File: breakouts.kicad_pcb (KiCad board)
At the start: 2 copper layers, 0 parts

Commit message: Start PCB placing
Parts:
- added C1001: 100nF, SMD0805, F.Cu at (107.0, 62.0)
- added C1101: 100nF, SMD0805, F.Cu at (93.0, 99.0)
- added C1102: 4.7uF, SMD0805, F.Cu at (99.0, 99.0)
- added C1103: 47pF, SMD0805, F.Cu at (106.0, 99.0)
- added C1104: 47pF, SMD0805, F.Cu at (112.0, 99.0)
- added C1105: 47pF, SMD0805, F.Cu at (117.0, 99.0)
- added C1201: 100nF, SMD0805, F.Cu at (163.0, 49.0)
- added C1202: 1000uF 25V, C_radial_10mm, F.Cu at (141.0, 20.0)
- added C1203: 100nF, SMD0805, F.Cu at (157.0, 49.0)
- added C1204: 1000uF 16V, C_radial_10mm, F.Cu at (153.0, 20.0)
- added C1205: 100nF, SMD0805, F.Cu at (151.0, 49.0)
- added C1206: 1000uF 16V, C_radial_10mm, F.Cu at (165.0, 20.0)
- added C1207: 100uF, SMD0805, F.Cu at (145.0, 49.0)
- added C1301: 22pF, SMD0805, F.Cu at (192.0, 21.0)
- added C1302: 22pF, SMD0805, F.Cu at (186.0, 21.0)
- added C1303: 100nF, SMD0805, F.Cu at (180.0, 21.0)
- added C201: 10uF, SMD0805, F.Cu at (35.0, 37.0)
- added C301: 100nF, SMD0805, F.Cu at (53.0, 63.0)
- added C302: 4.7uF, SMD0805, F.Cu at (47.0, 63.0)
- added C303: 47pF, SMD0805, F.Cu at (41.0, 63.0)
- added C304: 47pF, SMD0805, F.Cu at (37.0, 63.0)
- added C305: 47pF, SMD0805, F.Cu at (32.0, 63.0)
- added C401: 47pF, SMD0805, F.Cu at (56.0, 104.0)
- added C402: 0.01µF, SMD0805, F.Cu at (50.0, 104.0)
- added C403: 2.2µF, SMD0805, F.Cu at (43.0, 104.0)
- added C404: 1nF, SMD0805, F.Cu at (37.0, 104.0)
- added C405: 1.2pF, SMD0805, F.Cu at (32.0, 104.0)
- added C406: 27pF, SMD0805, F.Cu at (26.0, 104.0)
- added C407: 2.7pF, SMD0805, F.Cu at (20.0, 104.0)
- added C501: 22µF, SMD0805, F.Cu at (46.0, 119.0)
- added C502: Open, SMD0805, F.Cu at (41.0, 119.0)
- added C503: 22µF, SMD0805, F.Cu at (36.0, 119.0)
- added C601: 10µF, SMD0805, F.Cu at (34.0, 137.0)
- added C602: 10µF, SMD0805, F.Cu at (28.0, 137.0)
- added C701: 100nF, SMD0805, F.Cu at (50.0, 155.0)
- added C702: 100nF, SMD0805, F.Cu at (45.0, 155.0)
- added C703: 22pF, SMD0805, F.Cu at (39.0, 155.0)
- added C704: 22pF, SMD0805, F.Cu at (34.0, 155.0)
- added C801: 100nF, SMD0805, F.Cu at (54.0, 182.0)
- added C802: 100nF, SMD0805, F.Cu at (60.0, 182.0)
- added C803: 1uF, SMD0805, F.Cu at (66.0, 182.0)
- added C804: 22pF, SMD0805, F.Cu at (71.0, 182.0)
- added C805: 22pF, SMD0805, F.Cu at (76.0, 182.0)
- added C901: 100nF, SMD0805, F.Cu at (103.0, 36.0)
- added D1101: LED, LED-0805, F.Cu at (128.0, 95.0)
- added D1102: LED, LED-0805, F.Cu at (122.0, 95.0)
- added D201: PWR, LED-0805, F.Cu at (41.0, 28.0)
- added D202: 3V6, SOD123F, F.Cu at (22.0, 28.0)
- added D203: 3V6, SOD123F, F.Cu at (28.0, 28.0)
- added D301: LED, LED-0805, F.Cu at (34.0, 58.0)
- added D302: LED, LED-0805, F.Cu at (39.0, 58.0)
- added D501: DIODESCH, SOD-123, F.Cu at (42.0, 123.0)
- added D701: RESET, LED-0805, F.Cu at (52.0, 150.0)
- added D702: POWER, LED-0805, F.Cu at (58.0, 150.0)
- added D801: RESET, LED-0805, F.Cu at (84.0, 187.0)
- added D802: POWER, LED-0805, F.Cu at (79.0, 187.0)
- added D901: RESET, LED-0805, F.Cu at (115.0, 35.0)
- added D902: POWER, LED-0805, F.Cu at (110.0, 35.0)
- added IC901: ATTINY85-S, SOIC-8, F.Cu at (94.0, 23.0)
- added J1101: USB_MINI-B, mini-USB, F.Cu at (108.0, 86.0)
- added J1201: JACK_5P, JACK_3.5mm, F.Cu at (123.0, 39.0)
- added J201: USB_MINI-B, mini-USB, F.Cu at (26.0, 37.0)
- added J301: USB_MINI-B, mini-USB, F.Cu at (22.0, 61.0)
- added J401: SMA, PCBedge_SMA, F.Cu at (31.0, 90.0)
- added J801: USB_MINI-B, mini-USB, F.Cu at (93.0, 190.0)
- added K1201: CONN_3, pin_array_3x1, F.Cu at (166.0, 29.0)
- added K1301: CONN_3, pin_array_3x1, F.Cu at (195.0, 17.0)
- added K601: CONN_3, pin_array_3x1, F.Cu at (31.0, 132.0)
- added K801: CONN_3, pin_array_3x1, F.Cu at (36.0, 178.0)
- added L401: 100nH, SMD0805, F.Cu at (53.0, 98.0)
- added L402: 8.2nH, SMD0805, F.Cu at (47.0, 98.0)
- added L403: 22nH, SMD0805, F.Cu at (41.0, 98.0)
- added L501: 22µH, Shielded_inductor, F.Cu at (30.0, 119.0)
- added P1001: CONN_4, pin_array_4x1, F.Cu at (107.0, 69.0)
- added P1002: CONN_4, pin_array_4x1, F.Cu at (96.0, 69.0)
- added P1101: CONN_6, pin_array_6x1, F.Cu at (125.0, 84.0)
- added P1102: CONN_6, pin_array_6x1, F.Cu at (125.0, 89.0)
- added P1201: CONN_2, Screw_Terminal_Block_2P, F.Cu at (165.0, 40.0)
- added P1202: CONN_2, Screw_Terminal_Block_2P, F.Cu at (155.0, 40.0)
- added P1203: CONN_2, Screw_Terminal_Block_2P, F.Cu at (145.0, 40.0)
- added P1301: CONN_2, pin_array_2x1, F.Cu at (181.0, 25.0)
- added P201: CONN_2, pin_array_2x1, F.Cu at (34.0, 28.0)
- added P202: CONN_2, pin_array_2x1, F.Cu at (42.0, 34.0)
- added P203: CONN_2, pin_array_2x1, F.Cu at (50.0, 34.0)
- added P301: CONN_6, pin_array_6x1, F.Cu at (45.0, 72.0)
- added P302: CONN_6, pin_array_6x1, F.Cu at (45.0, 77.0)
- added P401: CONN_8, pin_array_8x1, F.Cu at (26.0, 109.0)
- added P402: CONN_8, pin_array_8x1, F.Cu at (47.0, 110.0)
- added P501: CONN_2, pin_array_2x1, F.Cu at (56.0, 123.0)
- added P502: CONN_2, pin_array_2x1, F.Cu at (49.0, 123.0)
- added P701: POWER, pin_array_8x1, F.Cu at (68.0, 164.0)
- added P702: PORT B, pin_array_8x1, F.Cu at (47.0, 164.0)
- added P703: PORT C, pin_array_8x1, F.Cu at (25.0, 164.0)
- added P704: PORT D, pin_array_8x1, F.Cu at (90.0, 164.0)
- added P705: ISP, pin_array_3x2, F.Cu at (58.0, 158.0)
- added P801: PORT B, pin_array_8x1, F.Cu at (69.0, 192.0)
- added P802: PORT C, pin_array_8x1, F.Cu at (48.0, 192.0)
- added P803: PORT D, pin_array_8x1, F.Cu at (26.0, 192.0)
- added P804: ISP, pin_array_3x2, F.Cu at (35.0, 186.0)
- added P901: CONN_8, pin_array_8x1, F.Cu at (99.0, 30.0)
- added P902: ISP, pin_array_3x2, F.Cu at (92.0, 36.0)
- added R1101: 270R, SMD0603, F.Cu at (92.0, 104.0)
- added R1102: 270R, SMD0603, F.Cu at (99.0, 104.0)
- added R1103: 0R, SMD0603, F.Cu at (105.0, 104.0)
- added R1104: 27R, SMD0603, F.Cu at (111.0, 104.0)
- added R1105: 27R, SMD0603, F.Cu at (117.0, 104.0)
- added R1201: 10k, SMD0603, F.Cu at (186.0, 32.0)
- added R1202: 8.2k, SMD0603, F.Cu at (192.0, 32.0)
- added R1301: 10k, SMD0603, F.Cu at (199.0, 32.0)
- added R1302: 2.2k, SMD0603, F.Cu at (205.0, 32.0)
- added R1303: 2.2k, SMD0603, F.Cu at (211.0, 32.0)
- added R201: 1k, SMD0603, F.Cu at (41.0, 47.0)
- added R202: 1k5, SMD0603, F.Cu at (36.0, 47.0)
- added R203: 68R, SMD0603, F.Cu at (30.0, 47.0)
- added R204: 68R, SMD0603, F.Cu at (25.0, 47.0)
- added R205: 1M, SMD0603, F.Cu at (20.0, 47.0)
- added R301: 270R, SMD0603, F.Cu at (53.0, 67.0)
- added R302: 270R, SMD0603, F.Cu at (47.0, 67.0)
- added R303: 0R, SMD0603, F.Cu at (42.0, 67.0)
- added R304: 27R, SMD0603, F.Cu at (37.0, 67.0)
- added R305: 27R, SMD0603, F.Cu at (32.0, 67.0)
- added R501: 0R, SMD0603, F.Cu at (36.0, 123.0)
- added R701: 1k, SMD0603, F.Cu at (46.0, 150.0)
- added R702: 1k, SMD0603, F.Cu at (41.0, 150.0)
- added R703: 10k, SMD0603, F.Cu at (35.0, 150.0)
- added R801: 22R, SMD0603, F.Cu at (72.0, 186.0)
- added R802: 22R, SMD0603, F.Cu at (68.0, 186.0)
- added R803: 1k, SMD0603, F.Cu at (54.0, 186.0)
- added R804: 1k, SMD0603, F.Cu at (59.0, 186.0)
- added R805: 10k, SMD0603, F.Cu at (64.0, 186.0)
- added R901: 1k, SMD0603, F.Cu at (93.0, 43.0)
- added R902: 1k, SMD0603, F.Cu at (98.0, 43.0)
- added R903: 10k, SMD0603, F.Cu at (104.0, 43.0)
- added SW701: SW_PUSH, PUSH_BUTTON-TECon, F.Cu at (78.0, 154.0)
- added SW801: SW_PUSH, PUSH_BUTTON-TECon, F.Cu at (45.0, 185.0)
- added SW901: SW_PUSH, PUSH_BUTTON-TECon, F.Cu at (108.0, 22.0)
- added U1001: SST25VF016B, SOIC-8, F.Cu at (97.0, 60.0)
- added U1101: FT230X-QFN, QFN-16, F.Cu at (95.0, 88.0)
- added U1201: TDA1517ATW, TSSOP-20, F.Cu at (152.0, 31.0)
- added U1301: MCP7940M, SOIC-8_Narrow_3.90mm, F.Cu at (205.0, 19.0)
- added U301: FT230X, SSOP-16, F.Cu at (24.0, 74.0)
- added U401: MRF49XA, TSSOP-16, F.Cu at (22.0, 97.0)
- added U501: SP6641A/B, SOT-23, F.Cu at (20.0, 121.0)
- added U601: NX1117C33Z, SOT223, F.Cu at (20.0, 134.0)
- added U701: ATMEGA88PA-A, TQFP32-0.8mm, F.Cu at (26.0, 154.0)
- added U801: ATMEGA32U2, TQFP32-0.8mm, F.Cu at (24.0, 184.0)
- added X1301: 32.768kHz, AB38T_Crystal, F.Cu at (197.0, 25.0)
- added X401: 10MHz, HC49US, F.Cu at (32.0, 98.0)
- added X701: 12MHz 18pF, HC49US, F.Cu at (67.0, 153.0)
- added X801: 16MHz 18pF, HC49US, F.Cu at (85.0, 181.0)
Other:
- board outline added: 100 x 100 mm

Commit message: Fix VCCxx power symbols and nets
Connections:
- C1001 pad 1: VCC -> VCC9
- C1101 pad 1: VCC -> VCC3
- C1102 pad 1: VCC -> VCC3
- C1201 pad 1: VCC -> VCC11
- C1202 pad 1: VCC -> VCC11
- C1303 pad 1: VCC -> VCC12
- C201 pad 1: VCC -> VCC1
- C301 pad 1: VCC -> VCC2
- C302 pad 1: VCC -> VCC2
- C401 pad 1: VCC -> VCC10
- C402 pad 1: VCC -> VCC10
- C403 pad 1: VCC -> VCC10
- C701 pad 1: VCC -> VCC6
- C702 pad 1: VCC -> VCC6
- C901 pad 1: VCC -> VCC8
- IC901 pad 8: VCC -> VCC8
- J201 pad 1: /mini-usb/VBUS -> VCC1
- L401 pad 1: VCC -> VCC10
- P1002 pad 4: VCC -> VCC9
- P1101 pad 1: VCC -> VCC3
- P1201 pad 1: VCC -> VCC11
- P1301 pad 1: VCC -> VCC12
- P301 pad 1: VCC -> VCC2
- P401 pad 1: VCC -> VCC10
- P402 pad 1: VCC -> VCC10
- P701 pad 1: VCC -> VCC6
- P701 pad 2: VCC -> VCC6
- P701 pad 3: VCC -> VCC6
- P705 pad 2: VCC -> VCC6
- P802 pad 1: VCC -> VCC7
- P804 pad 2: VCC -> VCC7
- P901 pad 1: VCC -> VCC8
- P902 pad 2: VCC -> VCC8
- R1103 pad 1: VCC -> VCC3
- R1201 pad 1: VCC -> VCC11
- R1301 pad 1: VCC -> VCC12
- R1302 pad 1: VCC -> VCC12
- R1303 pad 1: VCC -> VCC12
- R201 pad 1: /mini-usb/VBUS -> VCC1
- R202 pad 2: /mini-usb/VBUS -> VCC1
- R303 pad 1: VCC -> VCC2
- R701 pad 1: VCC -> VCC6
- R702 pad 1: VCC -> VCC6
- R703 pad 1: VCC -> VCC6
- R803 pad 1: VCC -> VCC7
- R804 pad 1: VCC -> VCC7
- R805 pad 1: VCC -> VCC7
- R901 pad 1: VCC -> VCC8
- R902 pad 1: VCC -> VCC8
- R903 pad 1: VCC -> VCC8
- U1001 pad 8: VCC -> VCC9
- U1101 pad 10: VCC -> VCC3
- U1201 pad 15: VCC -> VCC11
- U1201 pad 16: VCC -> VCC11
- U1301 pad 8: VCC -> VCC12
- U301 pad 12: VCC -> VCC2
- U401 pad 14: VCC -> VCC10
- U701 pad 18: VCC -> VCC6
- U701 pad 4: VCC -> VCC6
- U701 pad 6: VCC -> VCC6

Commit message: Fix VCCxx power symbols and nets
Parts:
- moved D202 163.5 mm to (177.8, 77.5), turned to 90 degrees
- moved R204 162.4 mm to (185.4, 72.4), turned to 270 degrees
- moved D203 160.2 mm to (180.3, 77.5), turned to 90 degrees
- moved R205 158.3 mm to (175.3, 77.7), turned to 90 degrees
- moved P201 156.4 mm to (185.4, 67.3), turned to 270 degrees
- moved R203 155.0 mm to (182.9, 72.4), turned to 270 degrees
- moved C201 151.0 mm to (182.9, 67.3), turned to 270 degrees
- moved J201 148.1 mm to (169.4, 73.9)
- moved R202 144.9 mm to (179.1, 69.8), turned to 90 degrees
- moved P203 140.6 mm to (184.2, 76.2)
- moved P202 137.4 mm to (175.3, 67.3), turned to 270 degrees
- moved D201 132.4 mm to (167.6, 66.5), turned to 180 degrees
- moved R201 131.9 mm to (171.4, 66.5), turned to 180 degrees
- moved R1201 22.7 mm to (163.4, 33.8)
- moved R1202 22.7 mm to (169.4, 33.8)
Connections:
- P201 pad 1: /mini-usb/VBUS -> VCC1
- P202 pad 1: /mini-usb/VBUS -> VCC1
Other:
- outline, holes or cut-outs redrawn

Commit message: Start placing component
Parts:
- added slot-10mm: VAL**, slot-10mm, F.Cu at (187.8, 72.5)
- added slot-10mm: VAL**, slot-10mm, F.Cu at (198.1, 71.9)
- moved U501 187.8 mm to (204.9, 88.0), turned to 270 degrees
- moved U601 184.5 mm to (193.0, 69.8)
- moved J301 183.2 mm to (176.3, 159.8)
- moved L501 182.9 mm to (210.2, 87.5), turned to 180 degrees
- moved R501 174.0 mm to (204.9, 80.9)
- moved C602 174.0 mm to (191.0, 76.2), turned to 180 degrees
- moved C503 173.7 mm to (204.9, 78.1), turned to 180 degrees
- moved D501 173.3 mm to (210.2, 81.4), turned to 180 degrees
- moved C601 172.2 mm to (195.1, 76.2)
- moved K601 170.6 mm to (193.0, 78.7), turned to 180 degrees
- moved D301 169.8 mm to (180.1, 144.5), turned to 180 degrees
- moved U301 169.6 mm to (176.3, 148.6), turned to 270 degrees
- moved C304 169.0 mm to (179.6, 153.7)
- moved R304 167.9 mm to (182.6, 150.6)
- moved C502 167.7 mm to (204.9, 83.4)
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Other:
- outline, holes or cut-outs redrawn

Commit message: More placing
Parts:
- moved IC901 117.2 mm to (179.3, 103.4)
- moved P1203 117.2 mm to (251.5, 88.9), turned to 90 degrees
- moved P902 115.8 mm to (179.3, 112.0)
- moved C1202 109.3 mm to (236.5, 73.2), turned to 180 degrees
- moved C1204 108.9 mm to (242.8, 81.5)
- moved R902 107.0 mm to (188.2, 100.6), turned to 270 degrees
- moved P1202 104.8 mm to (251.5, 81.0), turned to 90 degrees
- moved D902 104.7 mm to (188.2, 104.6), turned to 270 degrees
- moved R901 104.7 mm to (173.2, 110.2), turned to 270 degrees
- moved P901 104.5 mm to (179.3, 96.8), turned to 180 degrees
- moved J1201 104.0 mm to (224.5, 61.7), turned to 270 degrees
- moved SW901 100.9 mm to (167.6, 103.4), turned to 270 degrees
- moved C1206 100.0 mm to (236.5, 89.9)
- moved C901 99.0 mm to (179.3, 99.1), turned to 180 degrees
- moved D901 93.8 mm to (170.9, 110.2), turned to 90 degrees
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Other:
- net class Power added: clearance 0.254, trace_width 0.5, via_dia 0.889, via_drill 0.635
- net class Seeedstudio min added: clearance 0.1524, trace_width 0.1524, via_dia 0.8, via_drill 0.3
- rule trace_min: 0.254 -> 0.1524
- rule via_min_drill: 0.508 -> 0.3
- rule via_min_size: 0.889 -> 0.8

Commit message: more placement
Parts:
- moved X401 29.3 mm to (32.0, 127.3)
- moved L401 28.9 mm to (30.2, 115.8)
- moved C401 26.7 mm to (38.9, 124.5), turned to 270 degrees
- moved U401 25.7 mm to (32.0, 120.7)
- moved C407 23.0 mm to (40.9, 113.5), turned to 90 degrees
- moved C402 22.3 mm to (41.1, 124.5), turned to 270 degrees
- moved L402 20.3 mm to (37.3, 115.8)
- moved C403 17.8 mm to (26.7, 111.0), turned to 270 degrees
- moved J401 17.0 mm to (32.5, 106.9), turned to 90 degrees
- moved C404 16.3 mm to (40.6, 119.9), turned to 90 degrees
- moved L403 14.0 mm to (37.3, 111.5)
- moved C405 11.2 mm to (33.8, 115.1), turned to 90 degrees
- moved P401 10.7 mm to (23.5, 119.4), turned to 270 degrees
- moved C406 10.5 mm to (33.3, 111.5), turned to 180 degrees
- moved P402 9.91 mm to (43.8, 119.4), turned to 270 degrees

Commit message: Component placement done
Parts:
- added BMIS-203_Shield: VAL**, BMIS-203_Shield, F.Cu at (251.1, 151.1)
- added breakaway: VAL**, breakaway, F.Cu at (56.1, 110.2)
- added slot-10mm: VAL**, slot-10mm, F.Cu at (56.1, 117.9)
- added slot-10mm: VAL**, slot-10mm, F.Cu at (65.5, 123.2)
- moved P401 239.7 mm to (261.3, 149.5), turned to 90 degrees
- moved C403 236.7 mm to (258.1, 160.3)
- moved L401 229.5 mm to (256.2, 155.9), turned to 90 degrees
- moved J401 225.6 mm to (251.1, 162.8), turned to 270 degrees
- moved C406 224.0 mm to (252.4, 157.8), turned to 0 degrees
- moved C405 222.1 mm to (252.4, 154.0), turned to 0 degrees
- moved U401 221.9 mm to (252.2, 148.3), turned to 180 degrees
- moved X401 220.6 mm to (252.2, 141.7), turned to 180 degrees
- moved L403 215.7 mm to (248.0, 157.8), turned to 180 degrees
- moved L402 214.1 mm to (248.0, 154.0), turned to 180 degrees
- moved C401 208.3 mm to (246.1, 145.7), turned to 90 degrees
- moved C407 207.6 mm to (244.2, 155.9), turned to 270 degrees
- moved C404 205.9 mm to (244.2, 150.8), turned to 270 degrees
- moved C402 203.5 mm to (243.5, 145.7), turned to 90 degrees
- moved P402 199.5 mm to (241.0, 149.5), turned to 90 degrees
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
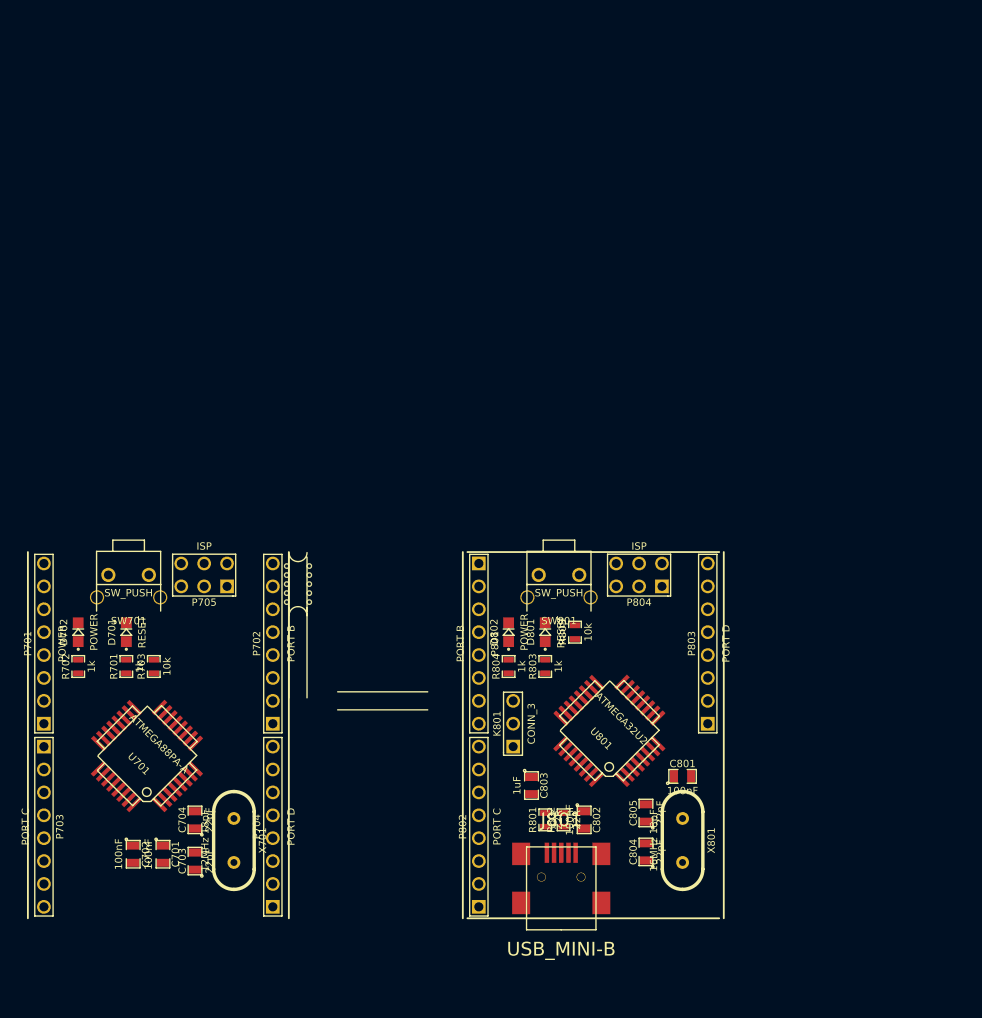
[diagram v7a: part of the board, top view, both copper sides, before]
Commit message: Begin slot/breakaway placement
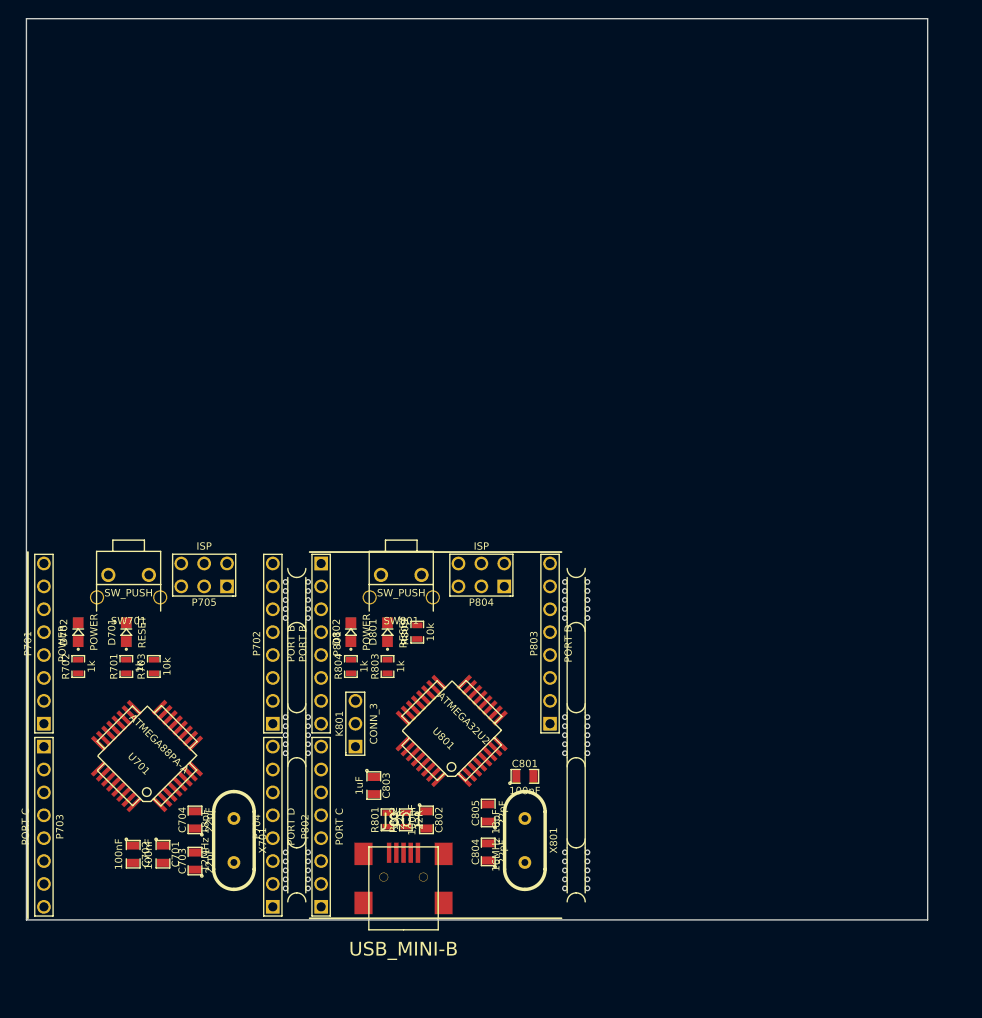
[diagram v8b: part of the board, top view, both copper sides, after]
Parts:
- removed the breakaway at (56.1, 110.2)
- added breakaway: VAL**, breakaway, F.Cu at (56.0, 112.0)
- added breakaway: VAL**, breakaway, F.Cu at (56.0, 127.0)
- added breakaway: VAL**, breakaway, F.Cu at (56.0, 142.0)
- added breakaway: VAL**, breakaway, F.Cu at (87.0, 112.0)
- added breakaway: VAL**, breakaway, F.Cu at (87.0, 127.0)
- added breakaway: VAL**, breakaway, F.Cu at (87.0, 142.0)
- added slot-10mm: VAL**, slot-10mm, F.Cu at (87.0, 119.5)
- added slot-10mm: VAL**, slot-10mm, F.Cu at (87.0, 134.5)
- moved K801 17.5 mm to (62.5, 125.7)
- moved C801 17.5 mm to (81.3, 131.6)
- moved C802 17.5 mm to (70.4, 136.4)
- moved C803 17.5 mm to (64.5, 132.6)
- moved C804 17.5 mm to (77.2, 140.0)
- moved C805 17.5 mm to (77.2, 135.6)
- moved D801 17.5 mm to (66.1, 115.6)
- moved J801 17.5 mm to (67.8, 142.7)
- moved P801 17.5 mm to (58.7, 116.8)
- moved P802 17.5 mm to (58.7, 137.2)
- moved P803 17.5 mm to (84.1, 116.8)
- moved P804 17.5 mm to (76.5, 109.2)
- moved R801 17.5 mm to (66.1, 136.4)
- moved R802 17.5 mm to (68.1, 136.4)
- moved R803 17.5 mm to (66.1, 119.4)
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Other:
- board size 100 x 100 mm -> 239 x 117.5 mm
